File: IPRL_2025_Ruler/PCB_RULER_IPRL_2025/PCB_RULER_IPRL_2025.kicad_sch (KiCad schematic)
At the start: 17 parts, among them J102 USB_C_Receptacle_PowerOnly_6P, U101 NE555D, U102 4017

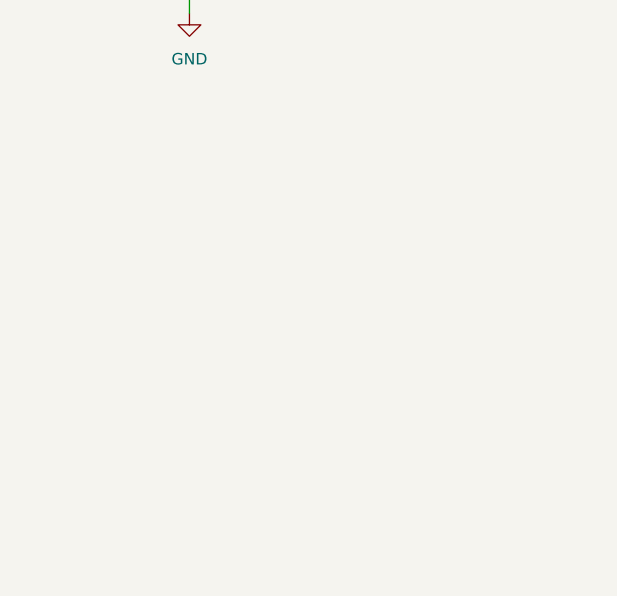
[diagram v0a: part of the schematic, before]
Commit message: Added NFC capabilities
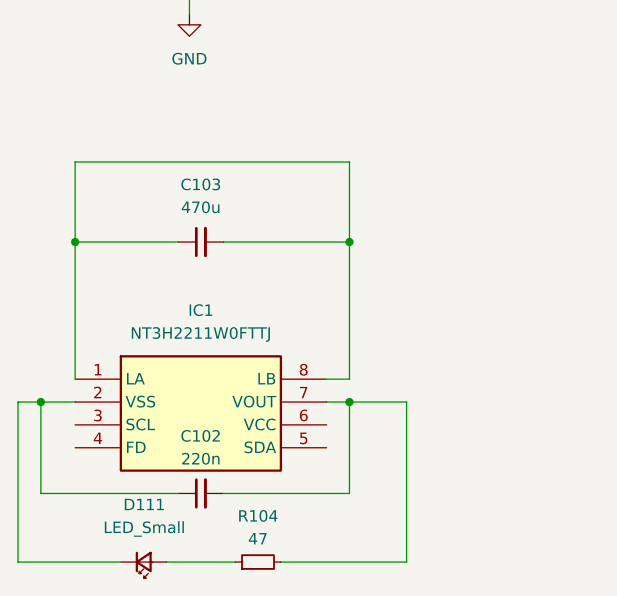
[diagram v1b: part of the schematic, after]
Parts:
- added C102: 220n, Capacitor_SMD:C_0402_1005Metric, symbol Device:C_Small
- added C103: 470u, Capacitor_SMD:C_0402_1005Metric, symbol Device:C_Small
- added D111: LED_Small, LED_SMD:LED_0402_1005Metric, symbol Device:LED_Small
- added IC1: NT3H2211W0FTTJ, SOP65P490X110-8N, symbol NT3H2211W0FTTJ:NT3H2211W0FTTJ
- added R104: 47, Resistor_SMD:R_0402_1005Metric, symbol Device:R_Small
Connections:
- new net: C103.1, C103.2, IC1.1 (LA), IC1.8 (LB)
- new net: C102.1, D111.1 (K), IC1.2 (VSS)
- new net: C102.2, IC1.7 (VOUT), R104.2
- new net: D111.2 (A), R104.1

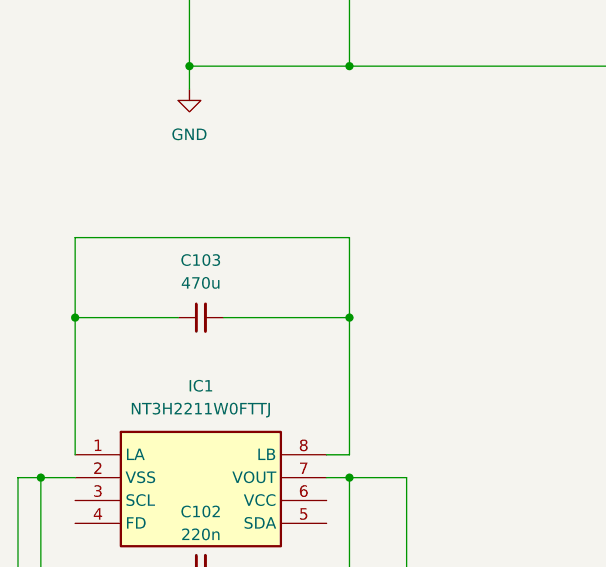
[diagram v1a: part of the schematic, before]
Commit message: Front side IPRL 2025 Ruler
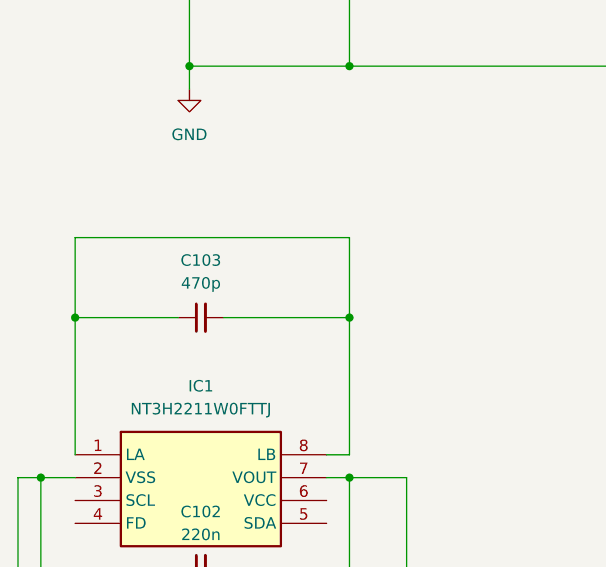
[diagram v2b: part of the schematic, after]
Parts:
- C103: value 470u -> 470p
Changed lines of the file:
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@@
 			)
 		)
-		(property "Value" "470u"
+		(property "Value" "470p"
 			(at 83.8263 134.62 90)
 			(effects

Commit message: Added member names
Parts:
- added D102: LED_Small, LED_SMD:LED_0402_1005Metric, symbol Device:LED_Small
- added R103: 430, Resistor_SMD:R_0402_1005Metric, symbol Device:R_Small
- renumbered C103 to C101, C101 to C103, D111 to D101, D109 to D103, D101 to D104, D108 to D105, D104 to D106, D110 to D107, D102 to D108, D103 to D109, D105 to D110, D106 to D111, D107 to D112, IC1 to IC101, J102 to J101, R104 to R101, R103 to R102, R101 to R104, R102 to R105
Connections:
- net +5V: now also R103.1
- net GND: now also D102.1 (K)
- new net: D102.2 (A), R103.2

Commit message: IPRL2025Ruler completed
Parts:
- R103: value 430 -> 470
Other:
- note added: "LED"
- note added: "NFC IC"
- moved on the sheet: C101, C102, D101, IC101, R101
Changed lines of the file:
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@@
 	(generator_version "9.0")
 	(paper "A4")
+	(rectangle
+		(start 57.785 139.7)
+		(end 109.22 193.04)
+		(stroke
+			(width 0)
+			(type default)
+		)
+		(fill
+			(type none)
+		)
+	)
+	(rectangle
+		(start 60.325 31.75)
+		(end 239.395 122.555)
+		(stroke
+			(width 0)
+			(type default)
+		)
+		(fill
+			(type none)
+		)
+	)
+	(text "LED"
+		(exclude_from_sim no)
+		(at 64.516 30.226 0)
+		(effects
+			(font
+				(face "Goldman")
+				(size 2.54 2.54)
+			)
+		)
+	)
+	(text "NFC IC"
+		(exclude_from_sim no)
+		(at 64.262 137.922 0)
+		(effects
+			(font
+				(face "Goldman")
+				(size 2.54 2.54)
+			)
+		)
+	)
 	(junction
 		(at 234.95 77.47)
@@
 	)
 	(junction
-		(at 66.04 156.21)
+		(at 66.04 168.91)
 		(diameter 0)
 		(color 0 0 0 0)
@@
 	)
 	(junction
-		(at 69.85 138.43)
+		(at 69.85 151.13)
 		(diameter 0)
 		(color 0 0 0 0)
@@
 	)
 	(junction
-		(at 100.33 138.43)
+		(at 100.33 151.13)
 		(diameter 0)
 		(color 0 0 0 0)
@@
 	)
 	(junction
-		(at 100.33 156.21)
+		(at 100.33 168.91)
 		(diameter 0)
 		(color 0 0 0 0)
@@
 	(wire
 		(pts
-			(xy 66.04 166.37) (xy 66.04 156.21)
+			(xy 66.04 179.07) (xy 66.04 168.91)
 		)
 		(stroke
@@
 	(wire
 		(pts
-			(xy 106.68 156.21) (xy 100.33 156.21)
+			(xy 106.68 168.91) (xy 100.33 168.91)
 		)
 		(stroke
@@
 	(wire
 		(pts
-			(xy 106.68 173.99) (xy 106.68 156.21)
+			(xy 106.68 186.69) (xy 106.68 168.91)
 		)
 		(stroke
@@
 	(wire
 		(pts
-			(xy 63.5 156.21) (xy 66.04 156.21)
+			(xy 63.5 168.91) (xy 66.04 168.91)
 		)
 		(stroke
@@
 	(wire
 		(pts
-			(xy 69.85 138.43) (xy 81.28 138.43)
+			(xy 69.85 151.13) (xy 81.28 151.13)
 		)
 		(stroke
@@
 	(wire
 		(pts
-			(xy 69.85 138.43) (xy 69.85 153.67)
+			(xy 69.85 151.13) (xy 69.85 166.37)
 		)
 		(stroke
@@
 	(wire
 		(pts
-			(xy 66.04 156.21) (xy 69.85 156.21)
+			(xy 66.04 168.91) (xy 69.85 168.91)
 		)
 		(stroke
@@
 	(wire
 		(pts
-			(xy 69.85 129.54) (xy 69.85 138.43)
+			(xy 69.85 142.24) (xy 69.85 151.13)
 		)
 		(stroke
@@
 	(wire
 		(pts
-			(xy 80.01 173.99) (xy 87.63 173.99)
+			(xy 80.01 186.69) (xy 87.63 186.69)
 		)
 		(stroke
@@
 	(wire
 		(pts
-			(xy 100.33 129.54) (xy 100.33 138.43)
+			(xy 100.33 142.24) (xy 100.33 151.13)
 		)
 		(stroke
@@
 	(wire
 		(pts
-			(xy 100.33 138.43) (xy 100.33 153.67)
+			(xy 100.33 151.13) (xy 100.33 166.37)
 		)
 		(stroke
@@
 	(wire
 		(pts
-			(xy 74.93 173.99) (xy 63.5 173.99)
+			(xy 74.93 186.69) (xy 63.5 186.69)
 		)
 		(stroke
@@
 	(wire
 		(pts
-			(xy 100.33 153.67) (xy 97.79 153.67)
+			(xy 100.33 166.37) (xy 97.79 166.37)
 		)
 		(stroke
@@
 	(wire
 		(pts
-			(xy 100.33 156.21) (xy 100.33 166.37)
+			(xy 100.33 168.91) (xy 100.33 179.07)
 		)
 		(stroke
@@
 	(wire
 		(pts
-			(xy 63.5 173.99) (xy 63.5 156.21)
+			(xy 63.5 186.69) (xy 63.5 168.91)
 		)
 		(stroke
@@
 	(wire
 		(pts
-			(xy 92.71 173.99) (xy 106.68 173.99)
+			(xy 92.71 186.69) (xy 106.68 186.69)
 		)
 		(stroke
@@
 	(wire
 		(pts
-			(xy 86.36 138.43) (xy 100.33 138.43)
+			(xy 86.36 151.13) (xy 100.33 151.13)
 		)
 		(stroke
@@
 	(wire
 		(pts
-			(xy 81.28 166.37) (xy 66.04 166.37)
+			(xy 81.28 179.07) (xy 66.04 179.07)
 		)
 		(stroke
@@
 	(wire
 		(pts
-			(xy 100.33 166.37) (xy 86.36 166.37)
+			(xy 100.33 179.07) (xy 86.36 179.07)
 		)
 		(stroke
@@
 	(wire
 		(pts
-			(xy 69.85 129.54) (xy 100.33 129.54)
+			(xy 69.85 142.24) (xy 100.33 142.24)
 		)
 		(stroke
@@
 	(wire
 		(pts
-			(xy 100.33 156.21) (xy 97.79 156.21)
+			(xy 100.33 168.91) (xy 97.79 168.91)
 		)
 		(stroke
@@
 	(symbol
 		(lib_id "NT3H2211W0FTTJ:NT3H2211W0FTTJ")
-		(at 69.85 153.67 0)
+		(at 69.85 166.37 0)
 		(unit 1)
 		(exclude_from_sim no)
@@
 		(fields_autoplaced yes)
 		(property "Reference" "IC101"
-			(at 83.82 146.05 0)
+			(at 83.82 158.75 0)
 			(effects
 				(font
@@
 		)
 		(property "Value" "NT3H2211W0FTTJ"
-			(at 83.82 148.59 0)
+			(at 83.82 161.29 0)
 			(effects
 				(font
@@
 		)
 		(property "Footprint" "SOP65P490X110-8N"
-			(at 93.98 248.59 0)
+			(at 93.98 261.29 0)
 			(effects
 				(font
@@
 		)
 		(property "Datasheet" "http://www.nxp.com/docs/en/data-sheet/NT3H2111_2211.pdf"
-			(at 93.98 348.59 0)
+			(at 93.98 361.29 0)
 			(effects
 				(font
@@
 		)
 		(property "Description" "RFID Transponders NTAG I C <i>plus</i> 2K, NFC Forum Type 2 Tag with I C interface optimized for entry-level NFC applications"
-			(at 69.85 153.67 0)
+			(at 69.85 166.37 0)
 			(effects
 				(font
@@
 		)
 		(property "Height" "1.1"
-			(at 93.98 548.59 0)
+			(at 93.98 561.29 0)
 			(effects
 				(font
@@
 		)
 		(property "Mouser Part Number" "771-NT3H2211W0FTTJ"
-			(at 93.98 648.59 0)
+			(at 93.98 661.29 0)
 			(effects
 				(font
@@
 		)
 		(property "Mouser Price/Stock" "https://www.mouser.co.uk/ProductDetail/NXP-Semiconductors/NT3H2211W0FTTJ?qs=5ptrxOxu%252BRZJZX9GB78j7w%3D%3D"
-			(at 93.98 748.59 0)
+			(at 93.98 761.29 0)
 			(effects
 				(font
@@
 		)
 		(property "Manufacturer_Name" "NXP"
-			(at 93.98 848.59 0)
+			(at 93.98 861.29 0)
 			(effects
 				(font
@@
 		)
 		(property "Manufacturer_Part_Number" "NT3H2211W0FTTJ"
-			(at 93.98 948.59 0)
+			(at 93.98 961.29 0)
 			(effects
 				(font
@@
 			)
 		)
-		(property "Value" "430"
+		(property "Value" "470"
 			(at 146.05 57.1499 0)
 			(effects
@@
 	(symbol
 		(lib_id "Device:C_Small")
-		(at 83.82 166.37 90)
+		(at 83.82 179.07 90)
 		(unit 1)
 		(exclude_from_sim no)
@@
 		(fields_autoplaced yes)
 		(property "Reference" "C102"
-			(at 83.8263 160.02 90)
+			(at 83.8263 172.72 90)
 			(effects
 				(font
@@
 		)
 		(property "Value" "220n"
-			(at 83.8263 162.56 90)
+			(at 83.8263 175.26 90)
 			(effects
 				(font
@@
 		)
 		(property "Footprint" "Capacitor_SMD:C_0402_1005Metric"
-			(at 83.82 166.37 0)
+			(at 83.82 179.07 0)
 			(effects
 				(font
@@
 		)
 		(property "Datasheet" "~"
-			(at 83.82 166.37 0)
+			(at 83.82 179.07 0)
 			(effects
 				(font
@@
 		)
 		(property "Description" "Unpolarized capacitor, small symbol"
-			(at 83.82 166.37 0)
+			(at 83.82 179.07 0)
 			(effects
 				(font
@@
 	(symbol
 		(lib_id "Device:R_Small")
-		(at 90.17 173.99 90)
+		(at 90.17 186.69 90)
 		(unit 1)
 		(exclude_from_sim no)
@@
 		(fields_autoplaced yes)
 		(property "Reference" "R101"
-			(at 90.17 168.91 90)
+			(at 90.17 181.61 90)
 			(effects
 				(font
@@
 		)
 		(property "Value" "47"
-			(at 90.17 171.45 90)
+			(at 90.17 184.15 90)
 			(effects
 				(font
@@
 		)
 		(property "Footprint" "Resistor_SMD:R_0402_1005Metric"
-			(at 90.17 173.99 0)
+			(at 90.17 186.69 0)
 			(effects
 				(font
@@
 		)
 		(property "Datasheet" "~"
-			(at 90.17 173.99 0)
+			(at 90.17 186.69 0)
 			(effects
 				(font
@@
 		)
 		(property "Description" "Resistor, small symbol"
-			(at 90.17 173.99 0)
+			(at 90.17 186.69 0)
 			(effects
 				(font
@@
 	(symbol
 		(lib_id "Device:LED_Small")
-		(at 77.47 173.99 0)
+		(at 77.47 186.69 0)
 		(mirror x)
 		(unit 1)
@@
 		(dnp no)
 		(property "Reference" "D101"
-			(at 77.5335 167.64 0)
+			(at 77.5335 180.34 0)
 			(effects
 				(font
@@
 		)
 		(property "Value" "LED_Small"
-			(at 77.5335 170.18 0)
+			(at 77.5335 182.88 0)
 			(effects
 				(font
@@
 		)
 		(property "Footprint" "LED_SMD:LED_0402_1005Metric"
-			(at 77.47 173.99 90)
+			(at 77.47 186.69 90)
 			(effects
 				(font
@@
 		)
 		(property "Datasheet" "~"
-			(at 77.47 173.99 90)
+			(at 77.47 186.69 90)
 			(effects
 				(font
@@
 		)
 		(property "Description" "Light emitting diode, small symbol"
-			(at 77.47 173.99 0)
+			(at 77.47 186.69 0)
 			(effects
 				(font
@@
 	(symbol
 		(lib_id "Device:C_Small")
-		(at 83.82 138.43 90)
+		(at 83.82 151.13 90)
 		(unit 1)
 		(exclude_from_sim no)
@@
 		(fields_autoplaced yes)
 		(property "Reference" "C101"
-			(at 83.8263 132.08 90)
+			(at 83.8263 144.78 90)
 			(effects
 				(font
@@
 		)
 		(property "Value" "470p"
-			(at 83.8263 134.62 90)
+			(at 83.8263 147.32 90)
 			(effects
 				(font
@@
 		)
 		(property "Footprint" "Capacitor_SMD:C_0402_1005Metric"
-			(at 83.82 138.43 0)
+			(at 83.82 151.13 0)
 			(effects
 				(font
@@
 		)
 		(property "Datasheet" "~"
-			(at 83.82 138.43 0)
+			(at 83.82 151.13 0)
 			(effects
 				(font
@@
 		)
 		(property "Description" "Unpolarized capacitor, small symbol"
-			(at 83.82 138.43 0)
+			(at 83.82 151.13 0)
 			(effects
 				(font
